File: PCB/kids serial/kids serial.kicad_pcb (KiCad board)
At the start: 2 copper layers, 76.2 x 43.2 mm, 6 parts, among them J1 n8 Bus Connector, J2 UARTConnector, J3 PowerViaUSB, U1 6551, X1 CXO_DIP14

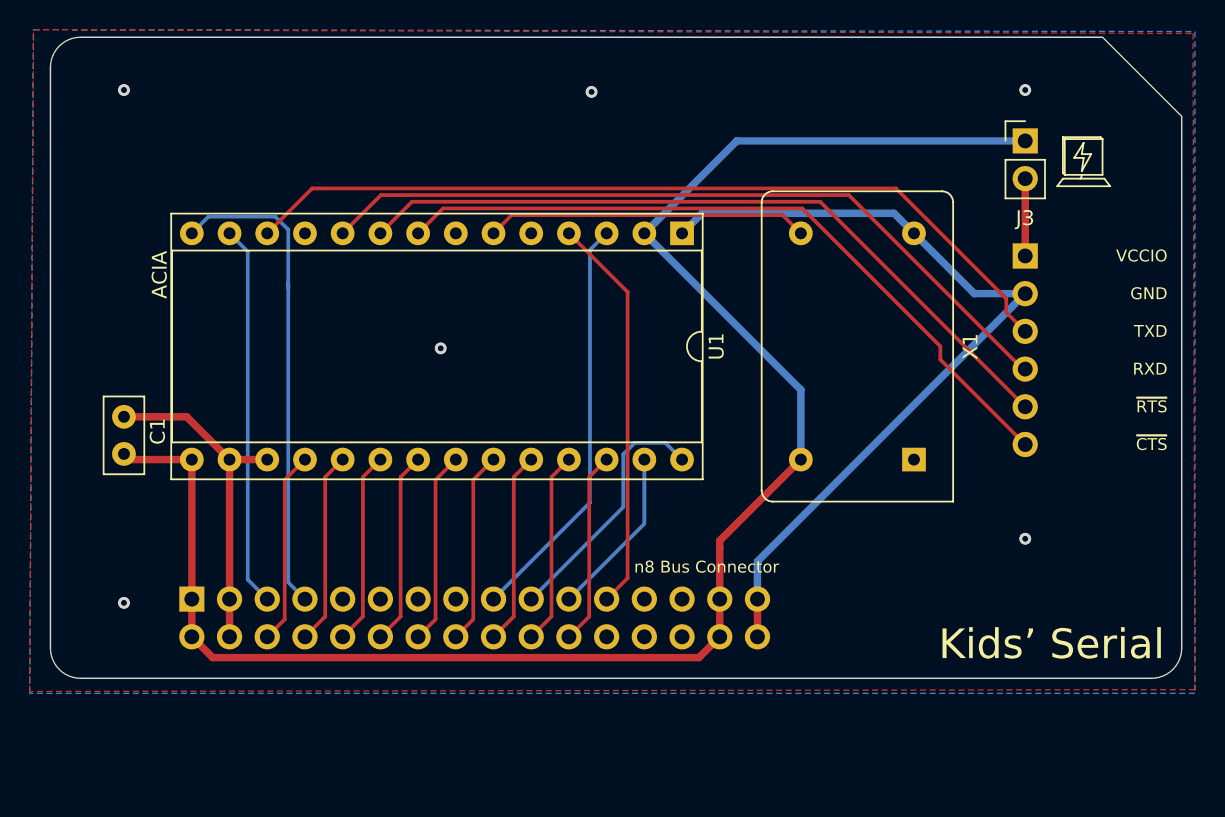
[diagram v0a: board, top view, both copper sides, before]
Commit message: New placement and parts for v2
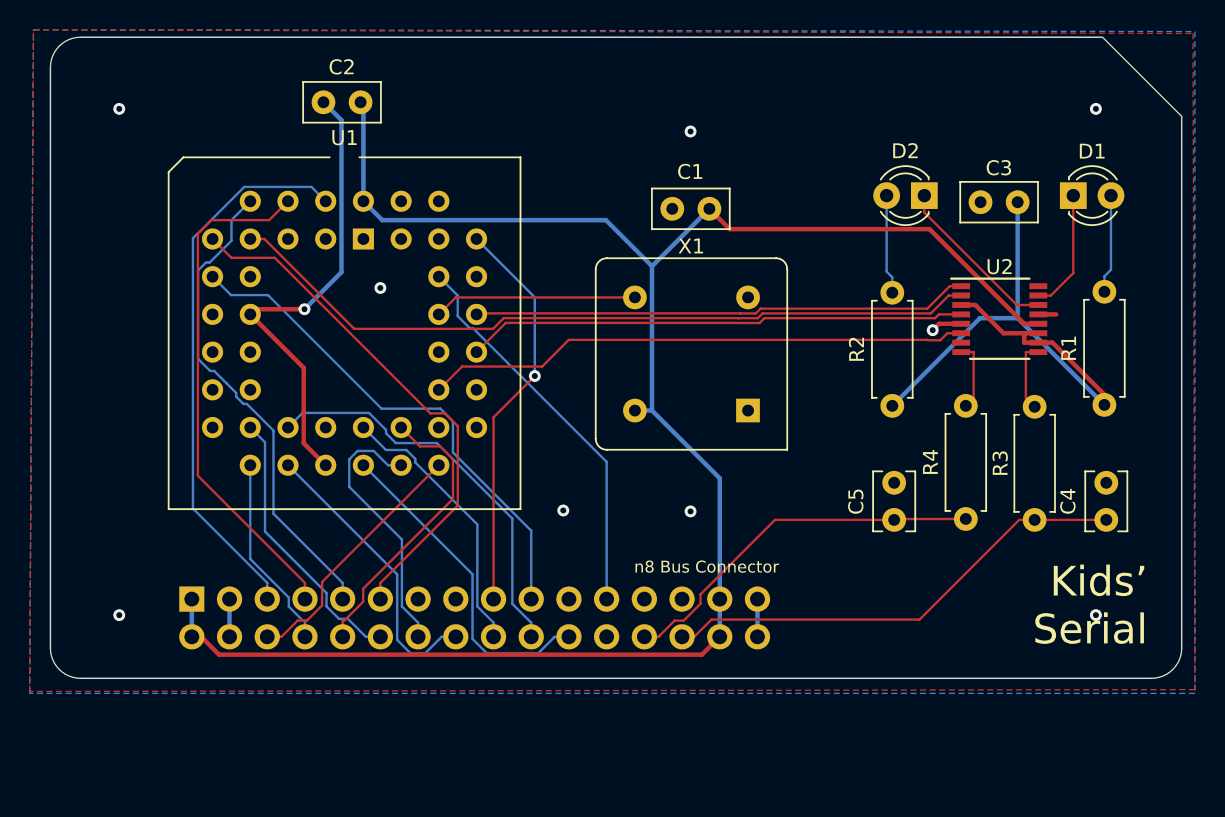
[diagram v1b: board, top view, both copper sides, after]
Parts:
- removed J2: UARTConnector, Connector_PinSocket_2.54mm:PinSocket_1x06_P2.54mm_Horizontal
- removed J3: PowerViaUSB, Connector_PinHeader_2.54mm:PinHeader_1x02_P2.54mm_Vertical
- added C2: 100nF, Capacitor_THT:C_Disc_D5.0mm_W2.5mm_P2.50mm, F.Cu at (121.5, 79.2)
- added C3: 100nF, Capacitor_THT:C_Disc_D5.0mm_W2.5mm_P2.50mm, F.Cu at (165.7, 85.9)
- added C4: 47pF, Capacitor_THT:C_Disc_D3.8mm_W2.6mm_P2.50mm, F.Cu at (171.7, 107.3)
- added C5: 47pF, Capacitor_THT:C_Disc_D3.8mm_W2.6mm_P2.50mm, F.Cu at (157.4, 107.3)
- added D1: TX, LED_THT:LED_D3.0mm, F.Cu at (169.5, 85.5)
- added D2: RX, LED_THT:LED_D3.0mm, F.Cu at (159.4, 85.5)
- added R1: 330, Resistor_THT:R_Axial_DIN0207_L6.3mm_D2.5mm_P7.62mm_Horizontal, F.Cu at (171.6, 99.6)
- added R2: 330, Resistor_THT:R_Axial_DIN0207_L6.3mm_D2.5mm_P7.62mm_Horizontal, F.Cu at (157.3, 99.6)
- added R3: 27, Resistor_THT:R_Axial_DIN0207_L6.3mm_D2.5mm_P7.62mm_Horizontal, F.Cu at (166.9, 99.7)
- added R4: 27, Resistor_THT:R_Axial_DIN0207_L6.3mm_D2.5mm_P7.62mm_Horizontal, F.Cu at (162.2, 99.6)
- added U2: FT230XS, Package_SO:SSOP-16_3.9x4.9mm_P0.635mm, F.Cu at (164.5, 93.8)
- C1: value 100nf -> 100nF
- U1: value 6551 -> SC28L92_PLC44; footprint Package_DIP:DIP-28_W15.24mm_Socket -> Package_LCC:PLCC-44_THT-Socket
- X1: value CXO_DIP14 -> 3.6864Mhz; footprint Oscillator:Oscillator_DIP-14 -> Oscillator:Oscillator_DIP-8
- moved C1 42.7 mm to (145.0, 86.4), turned to 180 degrees
- moved U1 21.5 mm to (121.7, 88.4), turned to 0 degrees
- moved X1 11.7 mm to (147.6, 99.9)
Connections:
- J1 pad 26: Net-(J1-Pad26) -> USB_D+
- J1 pad 28: Net-(J1-Pad28) -> USB_D-
- U1 pad 1: GND -> Net-(U1-Pad1)
- U1 pad 10: RXD_IO -> Net-(U1-Pad10)
- U1 pad 12: TXD_IO -> GND
- U1 pad 13: /A0 -> Net-(U1-Pad13)
- U1 pad 14: /A1 -> Net-(U1-Pad14)
- U1 pad 15: +5V -> Net-(U1-Pad15)
- U1 pad 16: GND -> Net-(U1-Pad16)
- U1 pad 17: GND -> Net-(U1-Pad17)
- U1 pad 18: /D0 -> /D1
- U1 pad 19: /D1 -> /D3
- U1 pad 2: +5V -> /A0
- U1 pad 20: /D2 -> /D5
- U1 pad 21: /D3 -> /D7
- U1 pad 22: /D4 -> GND
- U1 pad 23: /D5 -> Net-(U1-Pad23)
- U1 pad 24: /D6 -> ~IRQ
- U1 pad 25: /D7 -> /D6
- U1 pad 26: ~IRQ -> /D4
- U1 pad 27: CLK -> /D2
- U1 pad 28: R~W -> /D0
- U1 pad 3: ~CS -> Net-(U1-Pad3)
- U1 pad 4: ~RES -> /A1
- U1 pad 6: XTAL_CLK -> /A2
- U1 pad 7: Net-(U1-Pad7) -> /A3
- U1 pad 8: ~CTS_IO -> ~CTS
- U1 pad 9: ~RTS_IO -> R~W
- X1 pad 8: XTAL_CLK -> +5V
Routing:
- net TXD_IO: track 56.8 -> 0.00 mm
- net RXD_IO: track 51.9 -> 0.00 mm
- net ~CTS: track 0.00 -> 51.3 mm
- net ~RTS_IO: track 50.0 -> 0.00 mm
- net ~CTS_IO: track 48.7 -> 0.00 mm
- net +3V3: track 0.00 -> 41.1 mm
- net GND: track 79.3 -> 40.0 mm, vias 6 -> 10
- net ~RTS: track 0.00 -> 36.8 mm
- net /A3: track 0.00 -> 35.5 mm
- net TxD: track 0.00 -> 33.7 mm
- net RxD: track 0.00 -> 33.4 mm
- net /A2: track 0.00 -> 32.7 mm
- net USB_D-: track 0.00 -> 31.8 mm
- net USB_D+: track 0.00 -> 25.3 mm
- net R~W: track 17.1 -> 34.4 mm
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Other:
- net class Default: clearance 0.2 -> 0.16; trace_width 0.25 -> 0.16
- net class Power: clearance 0.3 -> 0.2; trace_width 0.5 -> 0.3
- rule trace_clearance: 0.2 -> 0.16
- rule trace_min: 0.2 -> 0.154
- board text removed: "ACIA"
- board text removed: "GND"
- board text removed: "RXD"
- board text removed: "TXD"
- board text removed: "VCCIO"
- board text removed: "~CTS"
- board text removed: "~RTS"

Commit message: v2 changes
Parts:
- removed C2, C3: 100nF, Capacitor_THT:C_Disc_D5.0mm_W2.5mm_P2.50mm
- removed C4, C5: 47pF, Capacitor_THT:C_Disc_D3.8mm_W2.6mm_P2.50mm
- removed D1: TX, LED_THT:LED_D3.0mm
- removed D2: RX, LED_THT:LED_D3.0mm
- removed R1, R2: 330, Resistor_THT:R_Axial_DIN0207_L6.3mm_D2.5mm_P7.62mm_Horizontal
- removed R3, R4: 27, Resistor_THT:R_Axial_DIN0207_L6.3mm_D2.5mm_P7.62mm_Horizontal
- removed U2: FT230XS, Package_SO:SSOP-16_3.9x4.9mm_P0.635mm
- added J2: UARTConnector, Connector_PinSocket_2.54mm:PinSocket_1x06_P2.54mm_Horizontal, B.Cu at (166.2, 89.5)
- added J3: PowerViaUSB, Connector_PinHeader_2.54mm:PinHeader_1x02_P2.54mm_Vertical, F.Cu at (166.2, 81.8)
- C1: value 100nF -> 100nf
- J1: moved to F.Cu
- U1: value SC28L92_PLC44 -> 6551; footprint Package_LCC:PLCC-44_THT-Socket -> Package_DIP:DIP-28_W15.24mm_Socket
- X1: value 3.6864Mhz -> CXO_DIP14; footprint Oscillator:Oscillator_DIP-8 -> Oscillator:Oscillator_DIP-14
- moved C1 42.7 mm to (105.5, 102.9), turned to 90 degrees
- moved J1 37.0 mm to (147.1, 112.6)
- moved U1 21.5 mm to (143.1, 88.0), turned to 270 degrees
- moved X1 11.7 mm to (158.8, 103.3)
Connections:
- J1 pad 1: +5V -> GND
- J1 pad 10: /D2 -> ~RES
- J1 pad 11: /A3 -> ~IRQ
- J1 pad 12: /D3 -> CLK
- J1 pad 13: /A4 -> /D7
- J1 pad 14: /D4 -> R~W
- J1 pad 15: /A5 -> /D6
- J1 pad 16: /D5 -> ~CS
- J1 pad 17: ~CS -> /D5
- J1 pad 18: /D6 -> /A5
- J1 pad 19: R~W -> /D4
- J1 pad 2: +5V -> GND
- J1 pad 20: /D7 -> /A4
- J1 pad 21: CLK -> /D3
- J1 pad 22: ~IRQ -> /A3
- J1 pad 23: ~RES -> /D2
- J1 pad 24: Net-(J1-Pad24) -> /A2
- J1 pad 25: Net-(J1-Pad25) -> /D1
- J1 pad 26: USB_D+ -> /A1
- J1 pad 27: Net-(J1-Pad27) -> /D0
- J1 pad 28: USB_D- -> /A0
- J1 pad 29: +5V -> GND
- J1 pad 3: GND -> +5V
- J1 pad 30: +5V -> GND
- J1 pad 31: GND -> +5V
- J1 pad 32: GND -> +5V
- J1 pad 4: GND -> +5V
- J1 pad 5: /A0 -> Net-(J1-Pad5)
- J1 pad 6: /D0 -> Net-(J1-Pad6)
- J1 pad 7: /A1 -> Net-(J1-Pad7)
- J1 pad 8: /D1 -> Net-(J1-Pad8)
- J1 pad 9: /A2 -> Net-(J1-Pad9)
- U1 pad 1: Net-(U1-Pad1) -> GND
- U1 pad 10: Net-(U1-Pad10) -> RXD_IO
- U1 pad 12: GND -> TXD_IO
- U1 pad 13: Net-(U1-Pad13) -> /A0
- U1 pad 14: Net-(U1-Pad14) -> /A1
- U1 pad 15: Net-(U1-Pad15) -> +5V
- U1 pad 16: Net-(U1-Pad16) -> GND
- U1 pad 17: Net-(U1-Pad17) -> GND
- U1 pad 18: /D1 -> /D0
- U1 pad 19: /D3 -> /D1
- U1 pad 2: /A0 -> +5V
- U1 pad 20: /D5 -> /D2
- U1 pad 21: /D7 -> /D3
- U1 pad 22: GND -> /D4
- U1 pad 23: Net-(U1-Pad23) -> /D5
- U1 pad 24: ~IRQ -> /D6
- U1 pad 25: /D6 -> /D7
- U1 pad 26: /D4 -> ~IRQ
- U1 pad 27: /D2 -> CLK
- U1 pad 28: /D0 -> R~W
- U1 pad 3: Net-(U1-Pad3) -> ~CS
- U1 pad 4: /A1 -> ~RES
- U1 pad 6: /A2 -> XTAL_CLK
- U1 pad 7: /A3 -> Net-(U1-Pad7)
- U1 pad 8: ~CTS -> ~CTS_IO
- U1 pad 9: R~W -> ~RTS_IO
- X1 pad 8: +5V -> XTAL_CLK
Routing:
- net TXD_IO: track 0.00 -> 56.8 mm
- net RXD_IO: track 0.00 -> 51.9 mm
- net ~CTS: track 51.3 -> 0.00 mm
- net ~RTS_IO: track 0.00 -> 50.0 mm
- net ~CTS_IO: track 0.00 -> 48.7 mm
- net +3V3: track 41.1 -> 0.00 mm
- net ~RTS: track 36.8 -> 0.00 mm
- net /A3: track 35.5 -> 0.00 mm
- net TxD: track 33.7 -> 0.00 mm
- net RxD: track 33.4 -> 0.00 mm
- net /A2: track 32.7 -> 0.00 mm
- net USB_D-: track 31.8 -> 0.00 mm
- net GND: track 40.0 -> 67.7 mm, vias 10 -> 5
- net USB_D+: track 25.3 -> 0.00 mm
- net /D7: track 27.1 -> 10.9 mm
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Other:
- net class Default: clearance 0.16 -> 0.2; trace_width 0.16 -> 0.25
- net class Power: clearance 0.2 -> 0.3; trace_width 0.3 -> 0.5
- rule trace_clearance: 0.16 -> 0.2
- rule trace_min: 0.154 -> 0.2
- board text added: "ACIA"
- board text added: "GND"
- board text added: "JLCJLCJLCJLC"
- board text added: "RXD"
- board text added: "TXD"
- board text added: "VCCIO"
- board text added: "~CTS"
- board text added: "~RTS"
